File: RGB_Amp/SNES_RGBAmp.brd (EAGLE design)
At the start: 18.4 x 16.5 mm, 9 parts

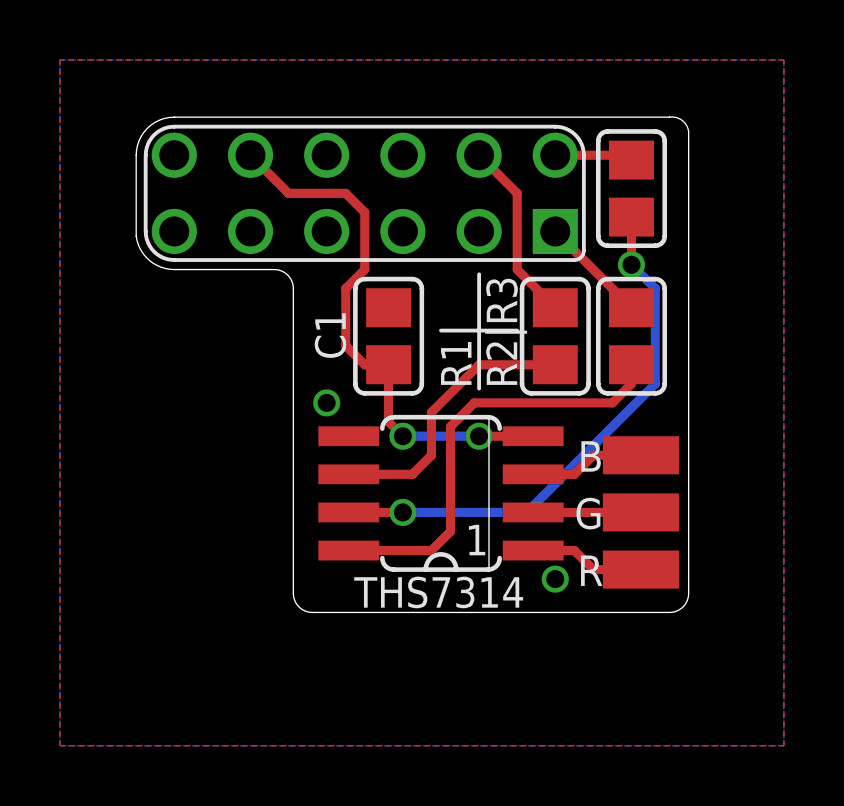
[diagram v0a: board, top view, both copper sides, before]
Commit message: Replace unused solder points at the MultiAV by simple holes
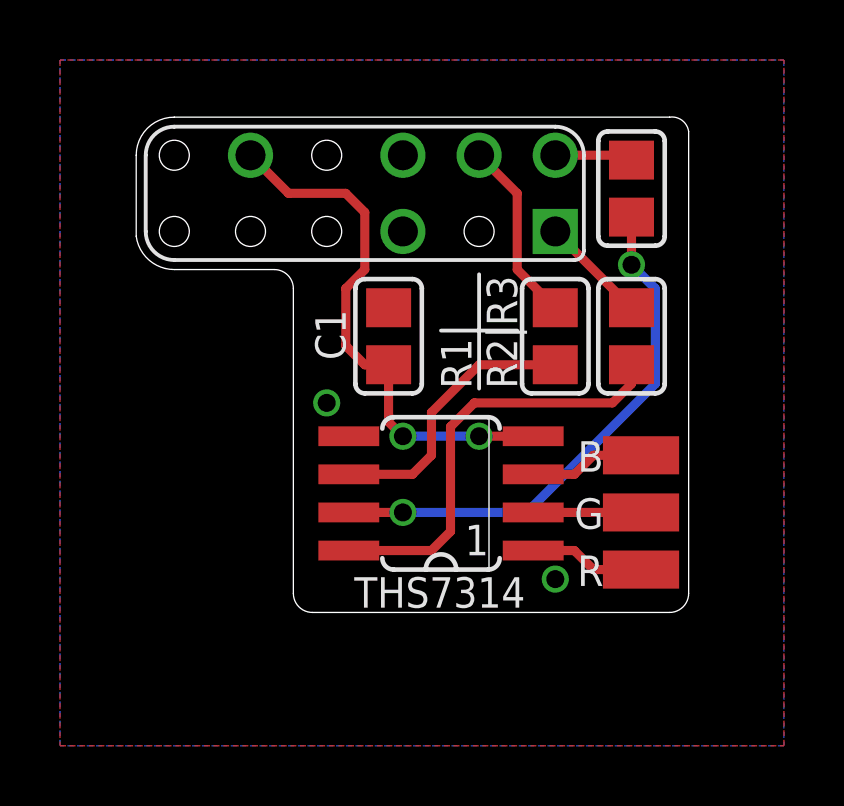
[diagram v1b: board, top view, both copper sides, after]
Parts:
- removed U$2: SNES_MULTIAV, snescart:SNES_MULTIAV
- added U$3: SNES_MULTIAV_RGB_ONLY, snes_div:SNES_MULTIAV_RGB_ONLY
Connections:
- net GND: now also U$3.P$5, U$3.P$6; no longer U$2.P$5, U$2.P$6
- net N$5: now also U$3.P$1; no longer U$2.P$1
- net N$6: now also U$3.P$2; no longer U$2.P$2
- net N$9: now also U$3.P$4; no longer U$2.P$4
- net VCC: now also U$3.P$10; no longer U$2.P$10
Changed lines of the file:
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@@
 <?xml version="1.0" encoding="utf-8"?>
 <!DOCTYPE eagle SYSTEM "eagle.dtd">
-<eagle version="6.5.0">
+<eagle version="7.0.0">
 <drawing>
 <settings>
@@
 <pass name="Default">
 <param name="RoutingGrid" value="50mil"/>
+<param name="AutoGrid" value="1"/>
+<param name="Efforts" value="0"/>
+<param name="TopRouterVariant" value="1"/>
 <param name="tpViaShape" value="round"/>
 <param name="PrefDir.1" value="|"/>
@@
 <elements>
 <element name="U$1" library="snescart" package="THS7314" value="THS7314" x="12.7" y="8.41375" smashed="yes" rot="R90"/>
-<element name="U$2" library="snescart" package="SNES_MULTIAV" value="SNES_MULTIAV" x="10.16" y="18.415"/>
 <element name="R2" library="snescart" package="Z0805" value="100" x="19.05" y="13.6525" smashed="yes" rot="R90"/>
 <element name="R3" library="snescart" package="Z0805" value="100" x="19.05" y="18.57375" smashed="yes" rot="R90"/>
@@
 <attribute name="NAME" x="18.11625" y="10.15375" size="1.016" layer="25" font="vector" ratio="12" rot="R180"/>
 </element>
+<element name="U$3" library="snes_div" package="SNES_MULTIAV_RGB_ONLY" value="SNES_MULTIAV_RGB_ONLY" x="10.16" y="18.415"/>
 </elements>
 <signals>
@@
 <signal name="N$6">
 <contactref element="R3" pad="2"/>
-<contactref element="U$2" pad="P$2"/>
-<wire x1="16.51" y1="19.685" x2="19.05" y2="19.685" width="0.3048" layer="1"/>
 <wire x1="19.05" y1="19.685" x2="19.05" y2="19.52375" width="0.3048" layer="1"/>
+<contactref element="U$3" pad="P$2"/>
+<wire x1="16.51" y1="19.685" x2="18.88875" y2="19.685" width="0.3048" layer="1"/>
+<wire x1="18.88875" y1="19.685" x2="19.05" y2="19.52375" width="0.3048" layer="1"/>
 </signal>
 <signal name="N$7">
@@
 <signal name="N$9">
 <contactref element="R1" pad="2"/>
-<contactref element="U$2" pad="P$4"/>
 <wire x1="16.51" y1="14.6025" x2="16.51" y2="14.605" width="0.3048" layer="1"/>
 <wire x1="16.51" y1="14.605" x2="15.24" y2="15.875" width="0.3048" layer="1"/>
 <wire x1="15.24" y1="15.875" x2="15.24" y2="18.415" width="0.3048" layer="1"/>
-<wire x1="15.24" y1="18.415" x2="13.97" y2="19.685" width="0.3048" layer="1"/>
+<contactref element="U$3" pad="P$4"/>
+<wire x1="13.97" y1="19.685" x2="15.24" y2="18.415" width="0.3048" layer="1"/>
 </signal>
 <signal name="GND">
-<contactref element="U$2" pad="P$6"/>
-<contactref element="U$2" pad="P$5"/>
 <contactref element="U$1" pad="5"/>
 <contactref element="C1" pad="2"/>
@@
 <via x="8.89" y="11.43" extent="1-16" drill="0.6"/>
 <via x="16.51" y="5.55625" extent="1-16" drill="0.6"/>
+<contactref element="U$3" pad="P$6"/>
+<contactref element="U$3" pad="P$5"/>
 </signal>
 <signal name="VCC">
-<contactref element="U$2" pad="P$10"/>
 <contactref element="U$1" pad="4"/>
 <contactref element="C1" pad="1"/>
@@
 <wire x1="10.95375" y1="10.795" x2="11.43" y2="10.31875" width="0.3048" layer="1"/>
 <wire x1="11.43" y1="10.31875" x2="13.97" y2="10.31875" width="0.3048" layer="16"/>
-<wire x1="6.35" y1="19.685" x2="7.62" y2="18.415" width="0.3048" layer="1"/>
 <wire x1="7.62" y1="18.415" x2="9.525" y2="18.415" width="0.3048" layer="1"/>
 <wire x1="9.525" y1="18.415" x2="10.16" y2="17.78" width="0.3048" layer="1"/>
@@
 <wire x1="10.16" y1="12.7" x2="10.95125" y2="12.7" width="0.3048" layer="1"/>
 <wire x1="10.95125" y1="12.7" x2="10.95375" y2="12.7025" width="0.3048" layer="1"/>
+<contactref element="U$3" pad="P$10"/>
+<wire x1="6.35" y1="19.685" x2="7.62" y2="18.415" width="0.3048" layer="1"/>
 </signal>
 <signal name="N$5">
 <contactref element="R2" pad="2"/>
-<contactref element="U$2" pad="P$1"/>
+<contactref element="U$3" pad="P$1"/>
 <wire x1="16.51" y1="17.145" x2="16.51" y2="17.1425" width="0.3048" layer="1"/>
 <wire x1="16.51" y1="17.1425" x2="19.05" y2="14.6025" width="0.3048" layer="1"/>

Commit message: Update silkscreen
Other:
- board text added: "RGBAmp V2.1 SNES/N64 by borti4938"
- board text added: "THS 7314"
- board text added: "borti4938"
- board text removed: "1"
- board text removed: "THS7314"
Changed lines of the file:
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@@
 <?xml version="1.0" encoding="utf-8"?>
 <!DOCTYPE eagle SYSTEM "eagle.dtd">
-<eagle version="7.0.0">
+<eagle version="6.5.0">
 <drawing>
 <settings>
@@
 <board>
 <plain>
-<text x="9.81075" y="4.60375" size="1.016" layer="21" font="vector" ratio="12">THS7314</text>
+<text x="13.97" y="6.6675" size="0.8128" layer="21" font="vector" ratio="15" rot="R90"> THS
+7314</text>
 <text x="15.24" y="11.90625" size="1.016" layer="25" font="vector" ratio="12" rot="R90">R1
 R2|R3</text>
@@
 <wire x1="20.32" y1="20.955" x2="3.81" y2="20.955" width="0" layer="20"/>
 <wire x1="2.54" y1="19.685" x2="2.54" y2="16.98625" width="0" layer="20"/>
-<text x="13.49375" y="6.35" size="1.016" layer="25" font="vector" ratio="12">1</text>
+<text x="8.73125" y="4.7625" size="1.016" layer="25" font="vector" ratio="12">borti4938</text>
 <wire x1="3.81" y1="15.875" x2="2.54" y2="16.98625" width="0" layer="20" curve="-82.371791"/>
 <wire x1="3.81" y1="20.955" x2="2.54" y2="19.685" width="0" layer="20" curve="90"/>
 <wire x1="13.97" y1="11.90625" x2="13.97" y2="15.71625" width="0.127" layer="25"/>
 <wire x1="12.7" y1="13.840734375" x2="15.24" y2="13.840734375" width="0.127" layer="25"/>
+<text x="19.812" y="11.27125" size="1.016" layer="22" font="vector" ratio="12" rot="MR0">RGBAmp V2.1
+ SNES/N64
+by borti4938</text>
 </plain>
 <attributes>
@@
 <pass name="Default">
 <param name="RoutingGrid" value="50mil"/>
-<param name="AutoGrid" value="1"/>
-<param name="Efforts" value="0"/>
-<param name="TopRouterVariant" value="1"/>
 <param name="tpViaShape" value="round"/>
 <param name="PrefDir.1" value="|"/>
@@
 <contactref element="U$1" pad="5"/>
 <contactref element="C1" pad="2"/>
-<polygon width="0.254" layer="1">
+<polygon width="0.254" layer="1" thermals="no">
 <vertex x="0" y="0"/>
 <vertex x="24.13" y="0"/>
@@
 <vertex x="0" y="22.86"/>
 </polygon>
-<polygon width="0.254" layer="16">
+<polygon width="0.254" layer="16" thermals="no">
 <vertex x="0" y="22.86"/>
 <vertex x="24.13" y="22.86"/>
